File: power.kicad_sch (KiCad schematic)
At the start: 10 parts, among them J20 Screw_Terminal_01x02, U6 AMS1117-3.3 SOT-223

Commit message: Most post v0.2.0 fixes done. About to mess with GND_ANT zone and net.
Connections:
- net +3V3: now also U6.4 (GND)
- net GND: no longer U6.4 (GND)
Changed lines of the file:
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@@
 	)
 	(junction
-		(at 152.4 80.01)
+		(at 144.78 87.63)
 		(diameter 0)
 		(color 0 0 0 0)
@@
 	(wire
 		(pts
+			(xy 144.78 80.01) (xy 144.78 87.63)
+		)
+		(stroke
+			(width 0)
+			(type default)
+		)
+	)
+	(wire
+		(pts
 			(xy 152.4 57.15) (xy 152.4 73.66)
 		)
@@
 	(wire
 		(pts
+			(xy 149.86 80.01) (xy 144.78 80.01)
+		)
+		(stroke
+			(width 0)
+			(type default)
+		)
+	)
+	(wire
+		(pts
 			(xy 152.4 73.66) (xy 152.4 78.74)
 		)
@@
 		(pts
 			(xy 121.92 116.84) (xy 121.92 118.11)
-		)
-		(stroke
-			(width 0)
-			(type default)
-		)
-	)
-	(wire
-		(pts
-			(xy 149.86 80.01) (xy 152.4 80.01)
 		)
 		(stroke
@@
 		(dnp no)
 		(property "Reference" "U6"
-			(at 141.224 82.296 0)
+			(at 159.512 81.534 0)
 			(effects
 				(font
@@
 		)
 		(property "Value" "AMS1117-3.3 SOT-223"
-			(at 139.7 84.582 0)
-			(effects
-				(font
+			(at 169.926 84.328 0)
+			(effects
+				(font

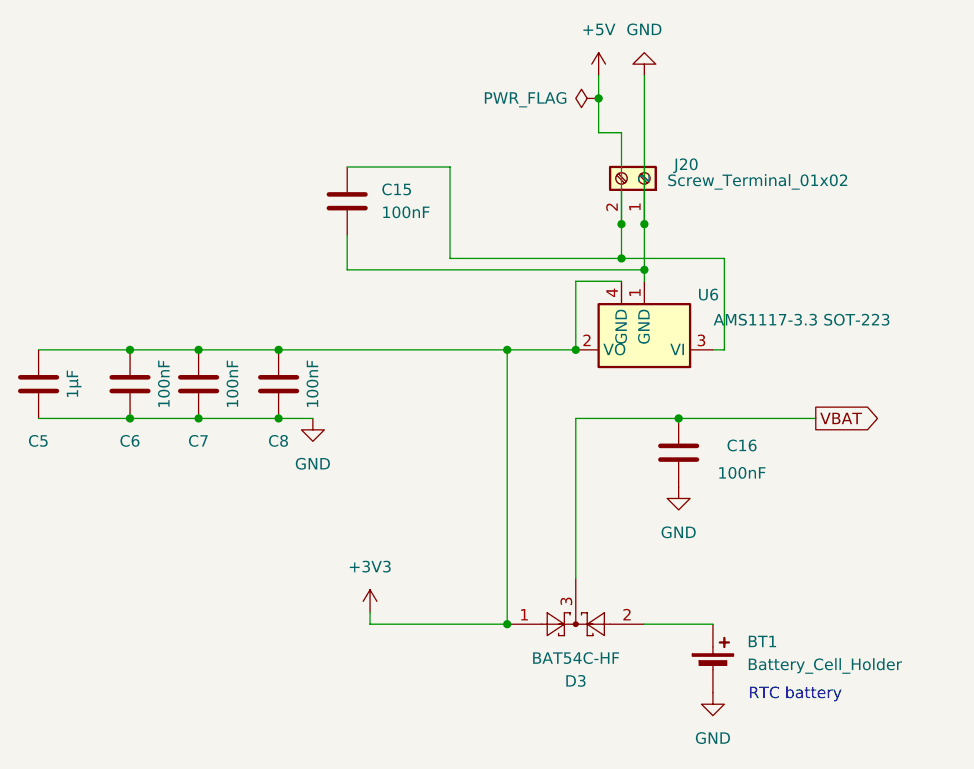
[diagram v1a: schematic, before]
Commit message: Added U.FL for antenna, with GND_ANT zone.
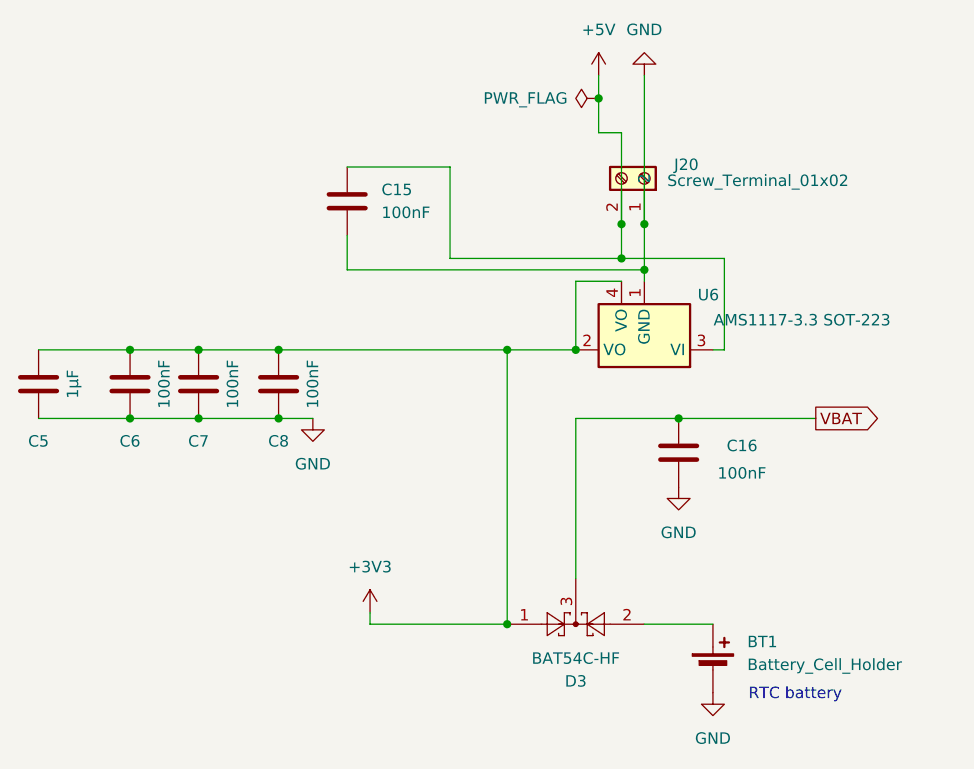
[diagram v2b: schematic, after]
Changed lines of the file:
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@@
 			)
 		)
-		(property "Datasheet" ""
+		(property "Datasheet" "~"
 			(at 111.76 91.44 0)
 			(effects
@@
 			)
 		)
-		(property "Datasheet" ""
+		(property "Datasheet" "~"
 			(at 102.87 91.44 0)
 			(effects
@@
 			)
 		)
-		(property "Datasheet" "https://www.te.com/commerce/DocumentDelivery/DDEController?Action=srchrtrv&DocNm=BAT-HLD-012-SMT&DocType=Data+Sheet&DocLang=English&DocFormat=pdf&PartCntxt=BAT-HLD-012-SMT"
+		(property "Datasheet" "~"
 			(at 160.02 121.666 90)
 			(effects
@@
 			)
 		)
-		(property "Description" "battery retainer coin 12mm smd"
+		(property "Description" "Single-cell battery"
 			(at 160.02 123.19 0)
 			(effects
@@
 			)
 		)
-		(property "Datasheet" ""
+		(property "Datasheet" "~"
 			(at 152.4 68.58 0)
 			(effects
@@
 			)
 		)
-		(property "Description" "Generic screw terminal, 01x02"
+		(property "Description" "Generic screw terminal, single row, 01x02, script generated (kicad-library-utils/schlib/autogen/connector/)"
 			(at 152.4 68.58 0)
 			(effects
@@
 			)
 		)
-		(property "Datasheet" ""
+		(property "Datasheet" "~"
 			(at 85.09 91.44 0)
 			(effects
@@
 			)
 		)
-		(property "Datasheet" "https://www.comchiptech.com/admin/files/product/QW-JB083%20BAT54-HF%20Series%20RevA.pdf"
+		(property "Datasheet" "http://www.diodes.com/_files/datasheets/ds11005.pdf"
 			(at 142.748 118.11 0)
 			(effects
@@
 			)
 		)
-		(property "Datasheet" ""
+		(property "Datasheet" "~"
 			(at 156.21 99.06 0)
 			(effects
@@
 			)
 		)
-		(property "Datasheet" ""
+		(property "Datasheet" "~"
 			(at 119.38 71.12 0)
 			(effects
@@
 			)
 		)
-		(property "Datasheet" ""
+		(property "Datasheet" "~"
 			(at 95.25 91.44 0)
 			(effects

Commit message: BOM cleaned up.
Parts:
- BT1: Package (none) -> BatteryHolder_LINX_BAT-HLD-012-SMT
- C15, C16, C5, C6, C7, C8: Notes (none) -> or equivalent; Package (none) -> C_0603_1608Metric
- D3: Package (none) -> SOT-23
- J20: Package (none) -> 1x02_P2.54mm_Horizontal
- U6: Package (none) -> SOT-223
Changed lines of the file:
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@@
+			)
+		)
+		(property "Package" "SOT-223"
+			(at 152.4 87.63 0)
+			(effects
+				(font
+					(size 1.27 1.27)
+				)
+				(hide yes)
 			)
 		)
@@
 			)
 		)
-		(property "Datasheet" "~"
+		(property "Datasheet" ""
 			(at 111.76 91.44 0)
 			(effects
@@
 		)
 		(property "MfgPart" "CL10B104KB8NNNC"
+			(at 111.76 91.44 0)
+			(effects
+				(font
+					(size 1.27 1.27)
+				)
+				(hide yes)
+			)
+		)
+		(property "Package" "C_0603_1608Metric"
+			(at 111.76 91.44 0)
+			(effects
+				(font
+					(size 1.27 1.27)
+				)
+				(hide yes)
+			)
+		)
+		(property "Notes" "or equivalent"
 			(at 111.76 91.44 0)
 			(effects
@@
 			)
 		)
-		(property "Datasheet" "~"
+		(property "Datasheet" ""
 			(at 102.87 91.44 0)
 			(effects
@@
 		)
 		(property "MfgPart" "CL10B104KB8NNNC"
+			(at 102.87 91.44 0)
+			(effects
+				(font
+					(size 1.27 1.27)
+				)
+				(hide yes)
+			)
+		)
+		(property "Package" "C_0603_1608Metric"
+			(at 102.87 91.44 0)
+			(effects
+				(font
+					(size 1.27 1.27)
+				)
+				(hide yes)
+			)
+		)
+		(property "Notes" "or equivalent"
 			(at 102.87 91.44 0)
 			(effects
@@
 			)
 		)
-		(property "Datasheet" "~"
+		(property "Datasheet" "https://www.te.com/commerce/DocumentDelivery/DDEController?Action=srchrtrv&DocNm=BAT-HLD-012-SMT&DocType=Data+Sheet&DocLang=English&DocFormat=pdf&PartCntxt=BAT-HLD-012-SMT"
 			(at 160.02 121.666 90)
 			(effects
@@
 			)
 		)
-		(property "Description" "Single-cell battery"
+		(property "Description" "12mm coin battery retainer smd"
 			(at 160.02 123.19 0)
 			(effects
@@
 		)
 		(property "pads" "3"
+			(at 160.02 123.19 0)
+			(effects
+				(font
+					(size 1.27 1.27)
+				)
+				(hide yes)
+			)
+		)
+		(property "Package" "BatteryHolder_LINX_BAT-HLD-012-SMT"
 			(at 160.02 123.19 0)
 			(effects
@@
 			)
 		)
-		(property "Datasheet" "~"
+		(property "Datasheet" ""
 			(at 152.4 68.58 0)
 			(effects
@@
 			)
 		)
-		(property "Description" "Generic screw terminal, single row, 01x02, script generated (kicad-library-utils/schlib/autogen/connector/)"
+		(property "Description" "Screw terminal 1x02"
 			(at 152.4 68.58 0)
 			(effects
@@
 					(size 1.27 1.27)
 				)
+			)
+		)
+		(property "Package" "1x02_P2.54mm_Horizontal"
+			(at 152.4 68.58 90)
+			(effects
+				(font
+					(size 1.27 1.27)
+				)
+				(hide yes)
 			)
 		)
@@
 			)
 		)
-		(property "Datasheet" "~"
+		(property "Datasheet" ""
 			(at 85.09 91.44 0)
 			(effects
@@
 		)
 		(property "MfgPart" "CL10A105KA8NNNC"
+			(at 85.09 91.44 0)
+			(effects
+				(font
+					(size 1.27 1.27)
+				)
+				(hide yes)
+			)
+		)
+		(property "Package" "C_0603_1608Metric"
+			(at 85.09 91.44 0)
+			(effects
+				(font
+					(size 1.27 1.27)
+				)
+				(hide yes)
+			)
+		)
+		(property "Notes" "or equivalent"
 			(at 85.09 91.44 0)
 			(effects
@@
 			)
 		)
+		(property "Package" "SOT-23"
+			(at 144.78 118.11 0)
+			(effects
+				(font
+					(size 1.27 1.27)
+				)
+				(hide yes)
+			)
+		)
 		(pin "2"
 		)
@@
 			)
 		)
-		(property "Datasheet" "~"
+		(property "Datasheet" ""
 			(at 156.21 99.06 0)
 			(effects
@@
 		)
 		(property "MfgPart" "CL10B104KB8NNNC"
+			(at 156.21 99.06 0)
+			(effects
+				(font
+					(size 1.27 1.27)
+				)
+				(hide yes)
+			)
+		)
+		(property "Package" "C_0603_1608Metric"
+			(at 156.21 99.06 0)
+			(effects
+				(font
+					(size 1.27 1.27)
+				)
+				(hide yes)
+			)
+		)
+		(property "Notes" "or equivalent"
 			(at 156.21 99.06 0)
 			(effects
@@
 			)
 		)
-		(property "Datasheet" "~"
+		(property "Datasheet" ""
 			(at 119.38 71.12 0)
 			(effects
@@
 		)
 		(property "MfgPart" "CL10B104KB8NNNC"
+			(at 119.38 71.12 0)
+			(effects
+				(font
+					(size 1.27 1.27)
+				)
+				(hide yes)
+			)
+		)
+		(property "Package" "C_0603_1608Metric"
+			(at 119.38 71.12 0)
+			(effects
+				(font
+					(size 1.27 1.27)
+				)
+				(hide yes)
+			)
+		)
+		(property "Notes" "or equivalent"
 			(at 119.38 71.12 0)
 			(effects
@@
 			)
 		)
-		(property "Datasheet" "~"
+		(property "Datasheet" ""
 			(at 95.25 91.44 0)
 			(effects
@@
 			(at 95.25 91.44 0)
 			(effects
+				(font
+					(size 1.27 1.27)
+				)
+				(hide yes)
+			)
+		)
+		(property "Package" "C_0603_1608Metric"
+			(at 95.25 91.44 0)
+			(effects
+				(font
+					(size 1.27 1.27)
+				)
+				(hide yes)
+			)
+		)
+		(property "Notes" "or equivalent"
+			(at 95.25 91.44 0)
+			(effects

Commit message: converted R, C, and L to smaller 0402 footprints. Some trace rearranging and cleanup.
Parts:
- C15, C16, C6, C7, C8: footprint ProjectLib:C_0603_1608Metric -> ProjectLib:C_0402_1005Metric; Manufacturer Samsung -> (none); MfgPart CL10B104KB8NNNC -> (none); Package C_0603_1608Metric -> C_0402_1005Metric
- C5: footprint ProjectLib:C_0603_1608Metric -> ProjectLib:C_0402_1005Metric; Manufacturer Samsung -> (none); MfgPart CL10A105KA8NNNC -> (none); Package C_0603_1608Metric -> C_0402_1005Metric
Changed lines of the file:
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@@
 			)
 		)
-		(property "Footprint" "ProjectLib:C_0603_1608Metric"
+		(property "Footprint" "ProjectLib:C_0402_1005Metric"
 			(at 110.7948 95.25 0)
 			(effects
@@
 			)
 		)
-		(property "Manufacturer" "Samsung"
+		(property "Manufacturer" ""
 			(at 111.76 91.44 0)
 			(effects
@@
 			)
 		)
-		(property "MfgPart" "CL10B104KB8NNNC"
+		(property "MfgPart" ""
 			(at 111.76 91.44 0)
 			(effects
@@
 			)
 		)
-		(property "Package" "C_0603_1608Metric"
+		(property "Package" "C_0402_1005Metric"
 			(at 111.76 91.44 0)
 			(effects
@@
 			)
 		)
-		(property "Footprint" "ProjectLib:C_0603_1608Metric"
+		(property "Footprint" "ProjectLib:C_0402_1005Metric"
 			(at 101.9048 95.25 0)
 			(effects
@@
 			)
 		)
-		(property "Manufacturer" "Samsung"
+		(property "Manufacturer" ""
 			(at 102.87 91.44 0)
 			(effects
@@
 			)
 		)
-		(property "MfgPart" "CL10B104KB8NNNC"
+		(property "MfgPart" ""
 			(at 102.87 91.44 0)
 			(effects
@@
 			)
 		)
-		(property "Package" "C_0603_1608Metric"
+		(property "Package" "C_0402_1005Metric"
 			(at 102.87 91.44 0)
 			(effects
@@
 			)
 		)
-		(property "Footprint" "ProjectLib:C_0603_1608Metric"
+		(property "Footprint" "ProjectLib:C_0402_1005Metric"
 			(at 84.1248 95.25 0)
 			(effects
@@
 			)
 		)
-		(property "Manufacturer" "Samsung"
+		(property "Manufacturer" ""
 			(at 85.09 91.44 0)
 			(effects
@@
 			)
 		)
-		(property "MfgPart" "CL10A105KA8NNNC"
+		(property "MfgPart" ""
 			(at 85.09 91.44 0)
 			(effects
@@
 			)
 		)
-		(property "Package" "C_0603_1608Metric"
+		(property "Package" "C_0402_1005Metric"
 			(at 85.09 91.44 0)
 			(effects
@@
 			)
 		)
-		(property "Footprint" "ProjectLib:C_0603_1608Metric"
+		(property "Footprint" "ProjectLib:C_0402_1005Metric"
 			(at 157.1752 102.87 0)
 			(effects
@@
 			)
 		)
-		(property "Manufacturer" "Samsung"
+		(property "Manufacturer" ""
 			(at 156.21 99.06 0)
 			(effects
@@
 			)
 		)
-		(property "MfgPart" "CL10B104KB8NNNC"
+		(property "MfgPart" ""
 			(at 156.21 99.06 0)
 			(effects
@@
 			)
 		)
-		(property "Package" "C_0603_1608Metric"
+		(property "Package" "C_0402_1005Metric"
 			(at 156.21 99.06 0)
 			(effects
@@
 			)
 		)
-		(property "Footprint" "ProjectLib:C_0603_1608Metric"
+		(property "Footprint" "ProjectLib:C_0402_1005Metric"
 			(at 120.3452 74.93 0)
 			(effects
@@
 			)
 		)
-		(property "Manufacturer" "Samsung"
+		(property "Manufacturer" ""
 			(at 119.38 71.12 0)
 			(effects
@@
 			)
 		)
-		(property "MfgPart" "CL10B104KB8NNNC"
+		(property "MfgPart" ""
 			(at 119.38 71.12 0)
 			(effects
@@
 			)
 		)
-		(property "Package" "C_0603_1608Metric"
+		(property "Package" "C_0402_1005Metric"
 			(at 119.38 71.12 0)
 			(effects
@@
 			)
 		)
-		(property "Footprint" "ProjectLib:C_0603_1608Metric"
+		(property "Footprint" "ProjectLib:C_0402_1005Metric"
 			(at 94.2848 95.25 0)
 			(effects
@@
 			)
 		)
-		(property "Manufacturer" "Samsung"
+		(property "Manufacturer" ""
 			(at 95.25 91.44 0)
 			(effects
@@
 			)
 		)
-		(property "MfgPart" "CL10B104KB8NNNC"
+		(property "MfgPart" ""
 			(at 95.25 91.44 0)
 			(effects
@@
 			)
 		)
-		(property "Package" "C_0603_1608Metric"
+		(property "Package" "C_0402_1005Metric"
 			(at 95.25 91.44 0)
 			(effects

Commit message: improved schematic sheet titles.
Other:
- title: ADCs for 10K thermistors -> Power Regulator & RTC Battery
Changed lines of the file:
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@@
 	(paper "A4")
 	(title_block
-		(title "ADCs for 10K thermistors")
-		(date "2025-01-07")
-		(rev "v0.1.1")
+		(title "Power Regulator & RTC Battery")
+		(date "2025-09-15")
+		(rev "v0.2.2")
 	)
 	(text "RTC battery"

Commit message: added new battery holder footprint.
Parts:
- BT1: footprint ProjectLib:BatteryHolder_LINX_BAT-HLD-012-SMT -> ProjectLib:BatteryHolder_CR1220_SMT
- D3: footprint ProjectLib:SOT-23 -> Package_TO_SOT_SMD:SOT-23
- U6: footprint ProjectLib:SOT-223 -> Package_TO_SOT_SMD:SOT-223-3_TabPin2
